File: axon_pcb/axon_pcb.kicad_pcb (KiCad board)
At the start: 2 copper layers, 227.6 x 99.2 mm, 125 parts, among them J1 USB_C_Receptacle, J2 AVR_ISP Header, K1 KEYSW, K10 KEYSW, K11 KEYSW, K12 KEYSW, K13 KEYSW, K14 KEYSW, K15 KEYSW, K16 KEYSW, K17 KEYSW, K18 KEYSW, K19 KEYSW, K2 KEYSW, K20 KEYSW, K21 KEYSW, K22 KEYSW, K23 KEYSW, K24 KEYSW, K25 KEYSW, K26 KEYSW, K27 KEYSW, K28 KEYSW, K29 KEYSW, K3 KEYSW, K30 KEYSW, K31 KEYSW, K32 KEYSW, K33 KEYSW, K34 KEYSW, K35 KEYSW, K36 KEYSW, K37 KEYSW, K38 KEYSW, K39 KEYSW, K4 KEYSW, K40 KEYSW, K41 KEYSW, K42 KEYSW, K43 KEYSW, K44 KEYSW, K45 KEYSW, K46 KEYSW, K5 KEYSW, K6 KEYSW, K7 KEYSW, K8 KEYSW, K9 KEYSW, SW1 RESET, SW2 BOOT, U1 ATmega328P-PU, X1 16MHz

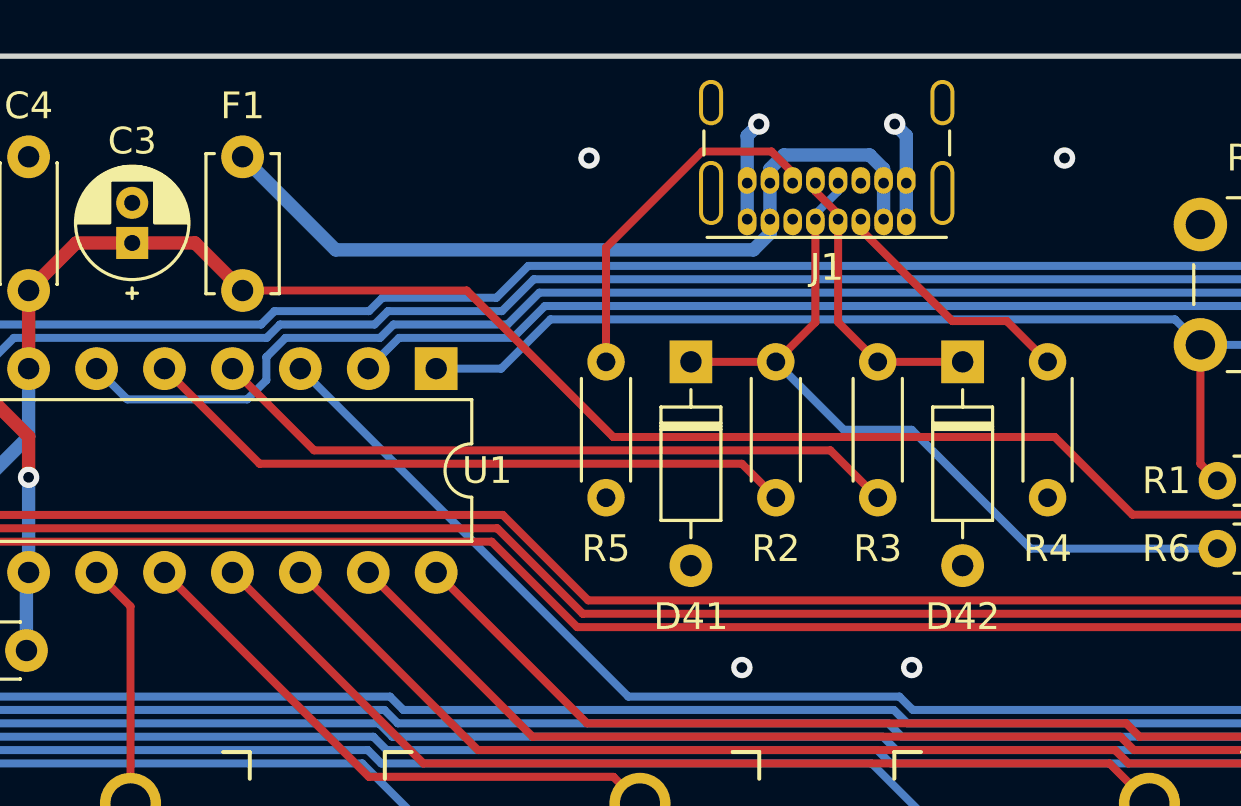
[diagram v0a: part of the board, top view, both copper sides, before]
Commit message: minor layout tweaks
- Increased compactness of components below USB connector
- Reduced length mismatch of USB data lines
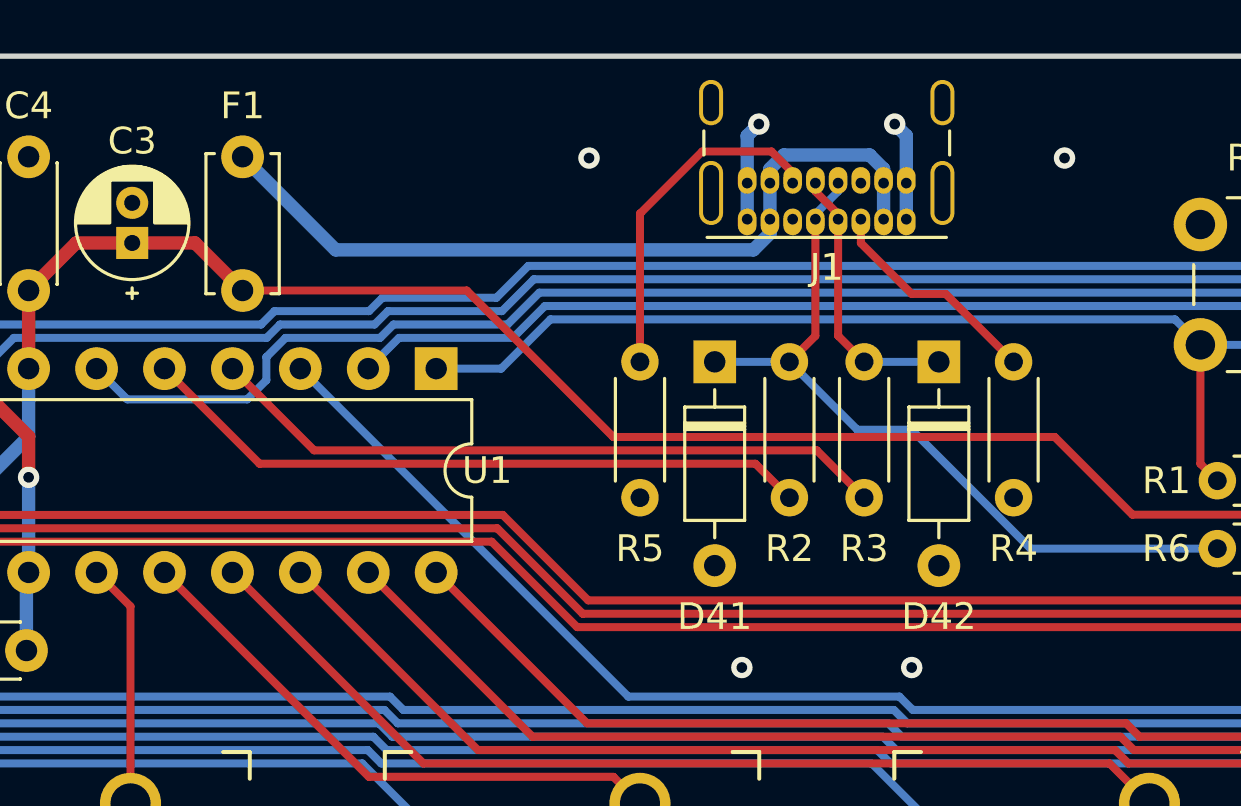
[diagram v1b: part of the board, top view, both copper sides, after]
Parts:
- moved R5 1.27 mm to (97.8, -16.5)
- moved R4 1.27 mm to (111.8, -16.5)
- moved D41 0.89 mm to (100.6, -21.6)
- moved D42 0.89 mm to (109.0, -21.6)
- moved R3 0.51 mm to (106.2, -16.5)
- moved R2 0.51 mm to (103.4, -16.5)
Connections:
- net Net-(D41-Pad1) renamed /D-
- net Net-(D42-Pad1) renamed /D+
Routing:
- net /D-: track 29.6 -> 28.5 mm
- net Net-(J1-PadA5): track 9.42 -> 8.44 mm
- net /D+: track 10.8 -> 10.2 mm
- net Net-(J1-PadB5): track 13.8 -> 13.3 mm
- net /USB_D+: track 26.1 -> 25.6 mm
- net /USB_D-: track 24.9 -> 25.4 mm

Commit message: minor routing change
- USB data line forced to pass directly through zener
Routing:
- net /D+: track 10.2 -> 11.4 mm
- net /D-: track 28.5 -> 29.6 mm

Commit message: minor grounding improvements
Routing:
- net GND: track 19.1 -> 27.1 mm, vias 30 -> 32

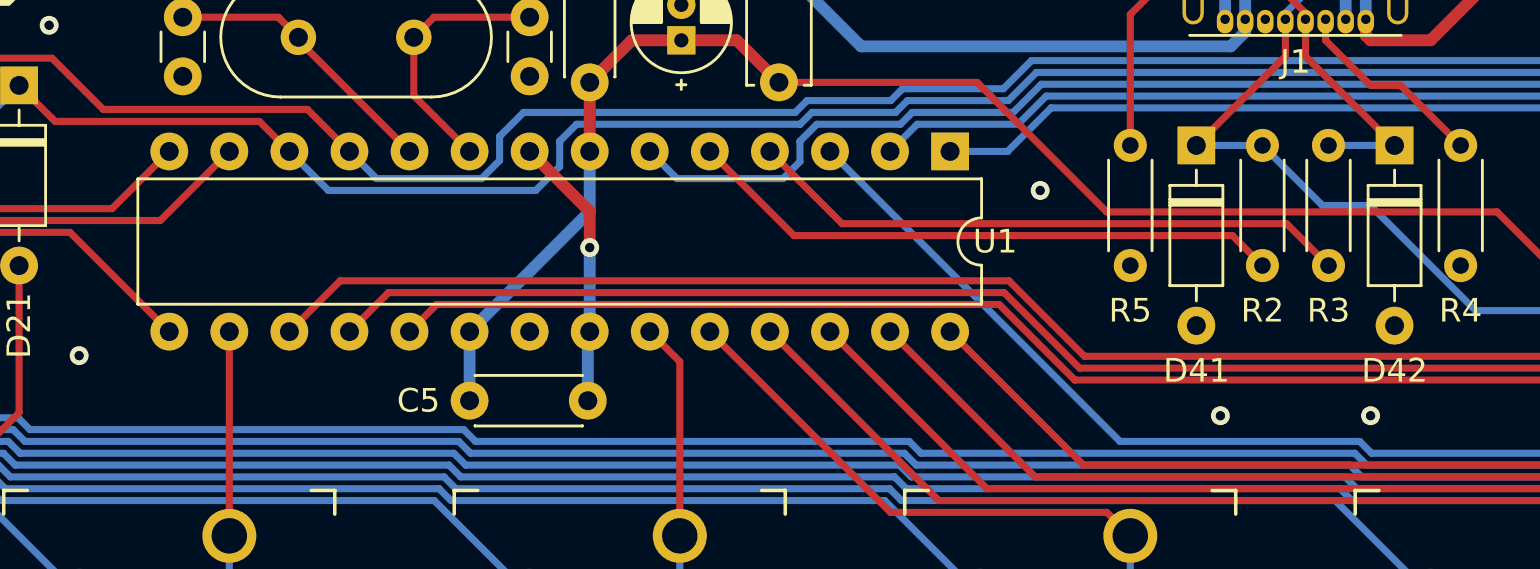
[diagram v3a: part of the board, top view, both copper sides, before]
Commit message: minor routing changes
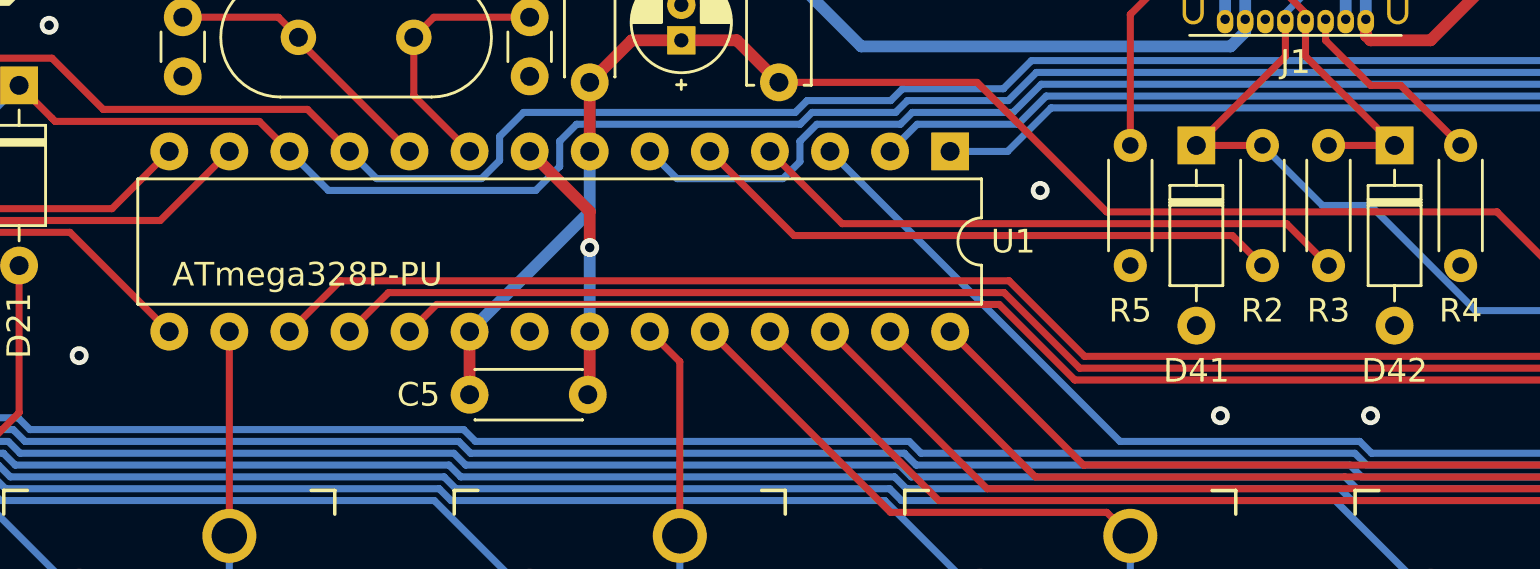
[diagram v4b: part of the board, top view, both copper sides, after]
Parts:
- F1: value 100mA -> 250mA
- moved C5 0.25 mm to (69.8, -11.0)
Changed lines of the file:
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@@
       (effects (font (size 1 1) (thickness 0.15)))
     )
-    (fp_text value 100mA (at 2.5 2.5 90) (layer F.Fab)
+    (fp_text value 250mA (at 2.5 2.5 90) (layer F.Fab)
       (effects (font (size 1 1) (thickness 0.15)))
     )
@@
   )
   (module Capacitor_THT:C_Disc_D4.3mm_W1.9mm_P5.00mm (layer F.Cu)
-    (at 69.85 -10.795)
+    (at 69.85 -11.049)
     (descr "C, Disc series, Radial, pin pitch=5.00mm, , diameter*width=4.3*1.9mm^2, Capacitor, http://www.vishay.com/docs/45233/krseries.pdf")
     (tags "C Disc series Radial pin pitch 5.00mm  diameter 4.3mm width 1.9mm Capacitor")
@@
     (descr "28-lead though-hole mounted DIP package, row spacing 7.62 mm (300 mils)")
     (tags "THT DIP DIL PDIP 2.54mm 7.62mm 300mil")
-    (fp_text reference U1 (at 3.81 -1.905 180) (layer F.SilkS)
+    (fp_text reference U1 (at 3.81 -2.667 180) (layer F.SilkS)
       (effects (font (size 1 1) (thickness 0.15)))
     )
-    (fp_text value ATmega328P-PU (at 3.81 35.35 90) (layer F.Fab)
+    (fp_text value ATmega328P-PU (at 5.207 27.178 180) (layer F.SilkS)
       (effects (font (size 1 1) (thickness 0.15)))
     )
@@
   (segment (start 101.79918 -30.04418) (end 102.235 -30.48) (width 0.5) (layer B.Cu) (net 56))
   (segment (start 101.79918 -28.274) (end 101.79918 -30.04418) (width 0.5) (layer B.Cu) (net 56))
-  (segment (start 74.85 -13.636) (end 74.93 -13.716) (width 0.5) (layer B.Cu) (net 56))
-  (segment (start 74.85 -10.795) (end 74.85 -13.636) (width 0.5) (layer B.Cu) (net 56))
   (via (at 93.98 -19.685) (size 0.8) (drill 0.4) (layers F.Cu B.Cu) (net 56))
   (via (at 115.57 -19.685) (size 0.8) (drill 0.4) (layers F.Cu B.Cu) (net 56))
@@
   (segment (start 110.49 -26.035) (end 113.665 -29.21) (width 0.5) (layer F.Cu) (net 56))
   (segment (start 107.95 -26.035) (end 110.49 -26.035) (width 0.5) (layer F.Cu) (net 56))
+  (segment (start 74.93 -11.129) (end 74.85 -11.049) (width 0.5) (layer F.Cu) (net 56))
+  (segment (start 74.93 -13.716) (end 74.93 -11.129) (width 0.5) (layer F.Cu) (net 56))
   (segment (start 62.611 -26.035) (end 62.611 -26.162) (width 0.3) (layer F.Cu) (net 57))
   (segment (start 67.31 -21.336) (end 62.611 -26.035) (width 0.3) (layer F.Cu) (net 57))
@@
   (segment (start 91.313 -24.257) (end 96.789979 -18.780021) (width 0.3) (layer F.Cu) (net 65))
   (segment (start 82.931 -24.257) (end 91.313 -24.257) (width 0.3) (layer F.Cu) (net 65))
-  (segment (start 69.85 -10.795) (end 69.85 -13.716) (width 0.5) (layer B.Cu) (net 65))
+  (segment (start 69.85 -13.716) (end 69.85 -11.049) (width 0.5) (layer F.Cu) (net 65))
   (segment (start 131.685601 -11.670601) (end 134.62 -14.605) (width 0.3) (layer F.Cu) (net 66))
   (segment (start 95.441401 -11.670601) (end 131.685601 -11.670601) (width 0.3) (layer F.Cu) (net 66))
@@
   (segment (start 107.95 -19.05) (end 112.395 -14.605) (width 0.3) (layer B.Cu) (net 73))
   (segment (start 112.395 -14.605) (end 118.745 -14.605) (width 0.3) (layer B.Cu) (net 73) (status 20))
-  (segment (start 100.584 -21.59) (end 103.378 -21.59) (width 0.3) (layer B.Cu) (net 73))
   (segment (start 105.918 -19.05) (end 107.95 -19.05) (width 0.3) (layer B.Cu) (net 73))
   (segment (start 103.378 -21.59) (end 105.918 -19.05) (width 0.3) (layer B.Cu) (net 73))
@@
   (segment (start 105.19918 -28.037071) (end 104.34918 -27.187071) (width 0.3) (layer B.Cu) (net 73))
   (segment (start 105.19918 -28.274) (end 105.19918 -28.037071) (width 0.3) (layer B.Cu) (net 73))
-  (segment (start 106.172 -21.59) (end 108.966 -21.59) (width 0.3) (layer B.Cu) (net 74))
+  (segment (start 100.584 -21.59) (end 103.378 -21.59) (width 0.3) (layer F.Cu) (net 73))
   (segment (start 105.19918 -25.35682) (end 108.966 -21.59) (width 0.3) (layer F.Cu) (net 74))
   (segment (start 105.19918 -26.924) (end 105.19918 -25.35682) (width 0.3) (layer F.Cu) (net 74))
@@
   (segment (start 104.34918 -28.037892) (end 105.19918 -27.187892) (width 0.3) (layer F.Cu) (net 74))
   (segment (start 104.34918 -28.274) (end 104.34918 -28.037892) (width 0.3) (layer F.Cu) (net 74))
+  (segment (start 108.966 -21.59) (end 106.172 -21.59) (width 0.3) (layer F.Cu) (net 74))
   (zone (net 56) (net_name GND) (layer F.Cu) (hatch edge 0.508)
     (connect_pads (clearance 0.508))

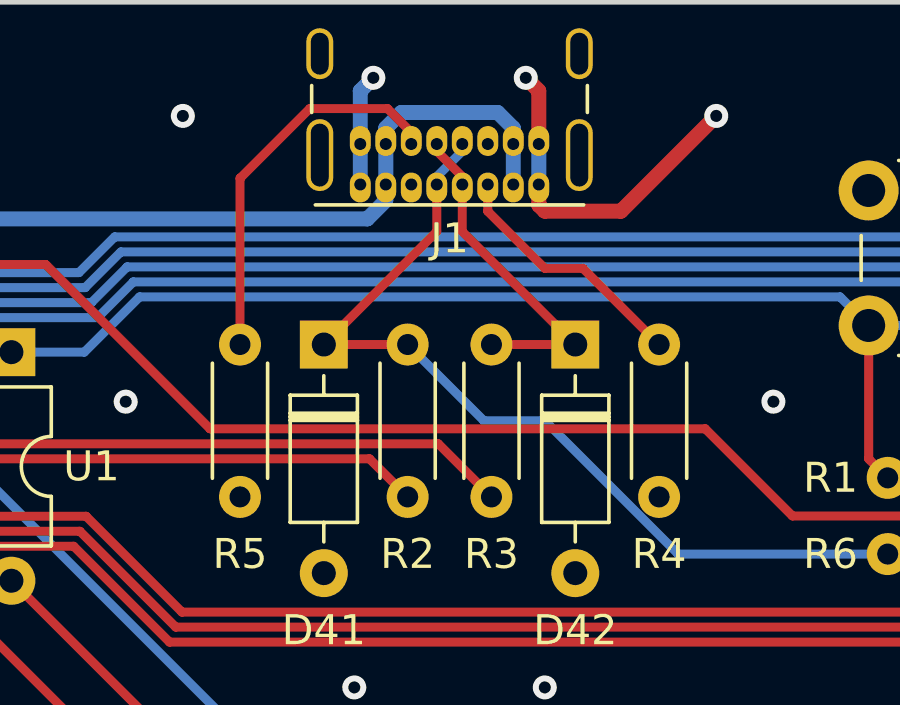
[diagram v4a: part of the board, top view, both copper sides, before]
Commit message: change resistor value
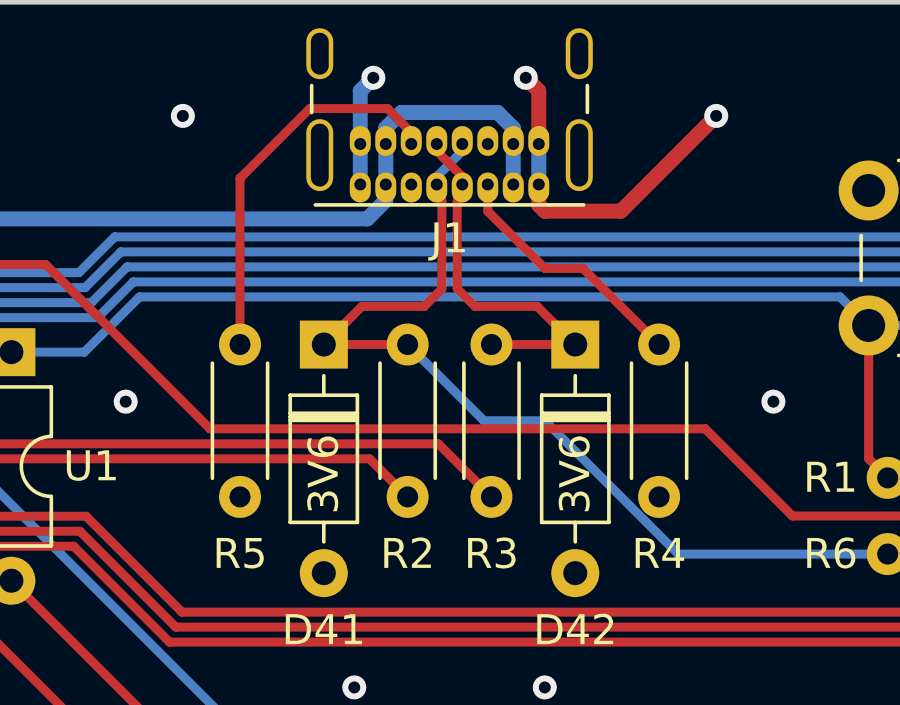
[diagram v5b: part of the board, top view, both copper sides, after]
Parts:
- R2, R3: value 75 -> 68
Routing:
- net /D-: track 29.6 -> 31.0 mm
- net /D+: track 11.4 -> 12.7 mm
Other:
- board text added: "3V6"
- board text added: "Designed by Robin L. Toronto, CA. 2021"
- board text removed: "Inspired by Gingham Designed by Robin L. Toronto, CA. 2021"
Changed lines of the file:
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@@
   (general
     (thickness 1.6)
-    (drawings 554)
-    (tracks 736)
+    (drawings 556)
+    (tracks 746)
     (zones 0)
     (modules 125)
@@
   )
   (setup
-    (last_trace_width 0.5)
+    (last_trace_width 0.25)
     (user_trace_width 0.3)
     (user_trace_width 0.5)
@@
       (effects (font (size 1 1) (thickness 0.15)))
     )
-    (fp_text value 75 (at 2.54 1.92 90) (layer F.Fab)
+    (fp_text value 68 (at 2.54 1.92 90) (layer F.Fab)
       (effects (font (size 1 1) (thickness 0.15)))
     )
@@
       (effects (font (size 1 1) (thickness 0.15)))
     )
-    (fp_text value 75 (at 2.54 1.92 90) (layer F.Fab)
+    (fp_text value 68 (at 2.54 1.92 90) (layer F.Fab)
       (effects (font (size 1 1) (thickness 0.15)))
     )
@@
     )
   )
+  (gr_text 3V6 (at 100.584 -17.272 90) (layer F.SilkS)
+    (effects (font (size 1 1) (thickness 0.15)))
+  )
+  (gr_text 3V6 (at 108.966 -17.272 90) (layer F.SilkS)
+    (effects (font (size 1 1) (thickness 0.15)))
+  )
   (dimension 99.170158 (width 0.15) (layer Dwgs.User)
     (gr_text "99.170 mm" (at -20.857999 16.56508 89.99999942) (layer Dwgs.User)
@@
     (effects (font (size 1.8 1.8) (thickness 0.3) italic) (justify mirror))
   )
-  (gr_text "Inspired by Gingham\nDesigned by\nRobin L.\nToronto, CA.\n2021" (at 148.59 -13.97) (layer B.SilkS)
+  (gr_text "Designed by\nRobin L.\nToronto, CA.\n2021" (at 148.59 -13.97) (layer B.SilkS)
     (effects (font (size 0.8 0.8) (thickness 0.15)) (justify mirror))
   )
@@
   (segment (start 105.918 -19.05) (end 107.95 -19.05) (width 0.3) (layer B.Cu) (net 73))
   (segment (start 103.378 -21.59) (end 105.918 -19.05) (width 0.3) (layer B.Cu) (net 73))
-  (segment (start 104.34918 -25.35518) (end 100.584 -21.59) (width 0.3) (layer F.Cu) (net 73))
-  (segment (start 104.34918 -26.924) (end 104.34918 -25.35518) (width 0.3) (layer F.Cu) (net 73))
   (segment (start 104.34918 -27.187071) (end 104.34918 -26.924) (width 0.3) (layer B.Cu) (net 73))
   (segment (start 105.19918 -28.037071) (end 104.34918 -27.187071) (width 0.3) (layer B.Cu) (net 73))
   (segment (start 105.19918 -28.274) (end 105.19918 -28.037071) (width 0.3) (layer B.Cu) (net 73))
   (segment (start 100.584 -21.59) (end 103.378 -21.59) (width 0.3) (layer F.Cu) (net 73))
-  (segment (start 105.19918 -25.35682) (end 108.966 -21.59) (width 0.3) (layer F.Cu) (net 74))
-  (segment (start 105.19918 -26.924) (end 105.19918 -25.35682) (width 0.3) (layer F.Cu) (net 74))
+  (segment (start 101.854 -22.86) (end 100.584 -21.59) (width 0.3) (layer F.Cu) (net 73))
+  (segment (start 103.93082 -22.86) (end 101.854 -22.86) (width 0.3) (layer F.Cu) (net 73))
+  (segment (start 104.521 -23.45018) (end 103.93082 -22.86) (width 0.3) (layer F.Cu) (net 73))
+  (segment (start 104.521 -26.362217) (end 104.521 -23.45018) (width 0.3) (layer F.Cu) (net 73))
+  (segment (start 104.49917 -26.384047) (end 104.521 -26.362217) (width 0.3) (layer F.Cu) (net 73))
+  (segment (start 104.49917 -26.77401) (end 104.49917 -26.384047) (width 0.3) (layer F.Cu) (net 73))
+  (segment (start 104.34918 -26.924) (end 104.49917 -26.77401) (width 0.3) (layer F.Cu) (net 73))
   (segment (start 105.19918 -27.187892) (end 105.19918 -26.924) (width 0.3) (layer F.Cu) (net 74))
   (segment (start 104.34918 -28.037892) (end 105.19918 -27.187892) (width 0.3) (layer F.Cu) (net 74))
   (segment (start 104.34918 -28.274) (end 104.34918 -28.037892) (width 0.3) (layer F.Cu) (net 74))
   (segment (start 108.966 -21.59) (end 106.172 -21.59) (width 0.3) (layer F.Cu) (net 74))
+  (segment (start 107.696 -22.86) (end 108.966 -21.59) (width 0.3) (layer F.Cu) (net 74))
+  (segment (start 105.029 -23.45182) (end 105.62082 -22.86) (width 0.3) (layer F.Cu) (net 74))
+  (segment (start 105.029 -26.363857) (end 105.029 -23.45182) (width 0.3) (layer F.Cu) (net 74))
+  (segment (start 105.04919 -26.384047) (end 105.029 -26.363857) (width 0.3) (layer F.Cu) (net 74))
+  (segment (start 105.62082 -22.86) (end 107.696 -22.86) (width 0.3) (layer F.Cu) (net 74))
+  (segment (start 105.04919 -26.77401) (end 105.04919 -26.384047) (width 0.3) (layer F.Cu) (net 74))
+  (segment (start 105.19918 -26.924) (end 105.04919 -26.77401) (width 0.3) (layer F.Cu) (net 74))
   (zone (net 56) (net_name GND) (layer F.Cu) (hatch edge 0.508)
     (connect_pads (clearance 0.508))
